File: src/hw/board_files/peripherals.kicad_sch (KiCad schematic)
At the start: 24 parts, among them J3 MSD-1-A, Q1 PMOS, U5 NEO-M9N, U6 BQ27427, U7 SHT30-DIS

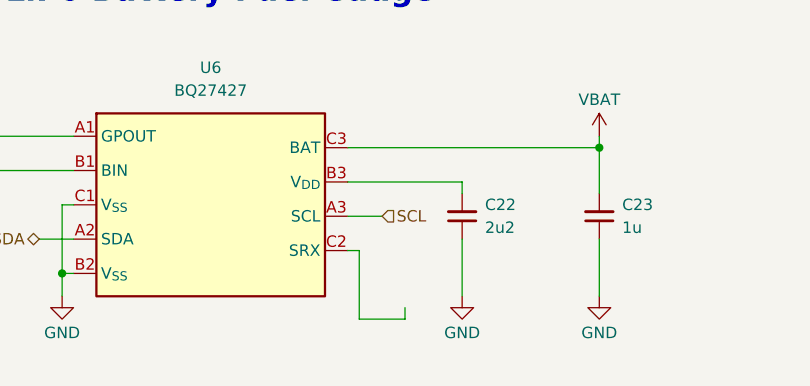
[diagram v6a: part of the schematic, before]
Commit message: Added more footprints and test points
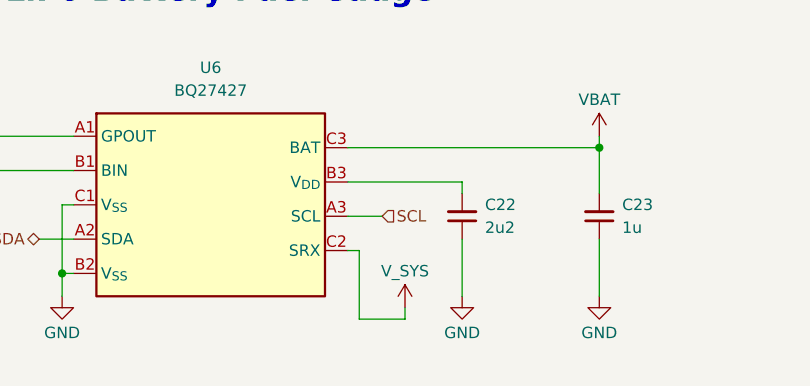
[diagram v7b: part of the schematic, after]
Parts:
- D7: footprint (none) -> LED_SMD:LED_0805_2012Metric_Pad1.15x1.40mm_HandSolder
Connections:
- net V_SYS: now reaches U6.C2 (SRX)
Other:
- title: Pocket Caddy -> Pocket Caddy - Golf GPS
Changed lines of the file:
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@@
 	(paper "A4")
 	(title_block
-		(title "Pocket Caddy")
-		(date "2025-09-25")
+		(title "Pocket Caddy - Golf GPS")
+		(date "2025-10-03")
 		(rev "0")
 		(company "EE 333 - Electronic Systems Design")
@@
 			)
 		)
-		(property "Footprint" ""
+		(property "Footprint" "LED_SMD:LED_0805_2012Metric_Pad1.15x1.40mm_HandSolder"
 			(at 52.07 69.85 0)
 			(effects
@@
 					(unit 1)
 				)
+			)
+		)
+	)
+	(symbol
+		(lib_id "power:+3V3")
+		(at 147.32 185.42 0)
+		(unit 1)
+		(exclude_from_sim no)
+		(in_bom yes)
+		(on_board yes)
+		(dnp no)
+		(property "Reference" "#PWR075"
+			(at 147.32 189.23 0)
+			(effects
+				(font
+					(size 1.27 1.27)
+				)
+				(hide yes)
+			)
+		)
+		(property "Value" "V_SYS"
+			(at 147.32 181.356 0)
+			(effects
+				(font
+					(size 1.27 1.27)
+				)
+			)
+		)
+		(property "Footprint" ""
+			(at 147.32 185.42 0)
+			(effects
+				(font
+					(size 1.27 1.27)
+				)
+				(hide yes)
+			)
+		)
+		(property "Datasheet" ""
+			(at 147.32 185.42 0)
+			(effects
+				(font
+					(size 1.27 1.27)
+				)
+				(hide yes)
+			)
+		)
+		(property "Description" "Power symbol creates a global label with name \"+3V3\""
+			(at 147.32 185.42 0)
+			(effects
+				(font
+					(size 1.27 1.27)
+				)
+				(hide yes)
+			)
+		)
+		(pin "1"
+		)
+		(instances
+			(project "pocket-caddy"
+				(path "/2c77a8ba-b277-4959-adec-d3fc778c7960/81382524-b053-4c3c-9e13-c8b314c52639"
+					(reference "#PWR075")
+					(unit 1)
+				)

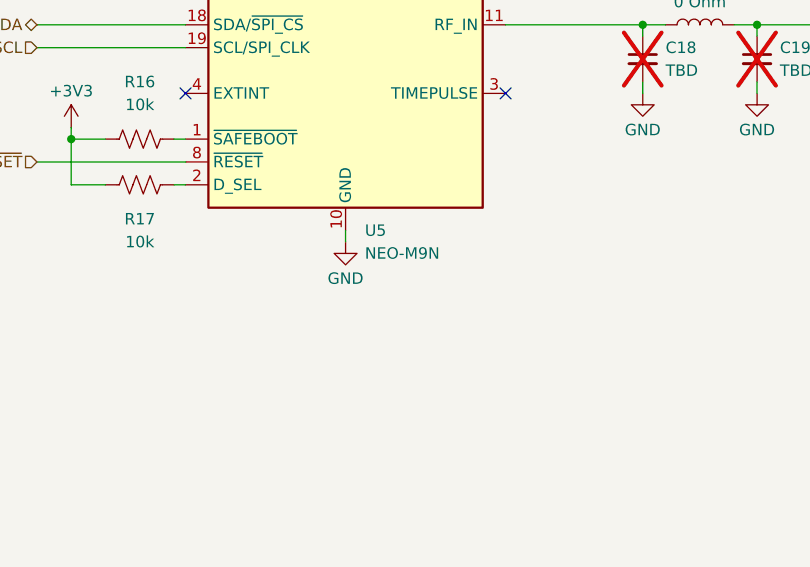
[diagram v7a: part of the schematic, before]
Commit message: Started Layout. Still Need Antenna & LCD Screen added
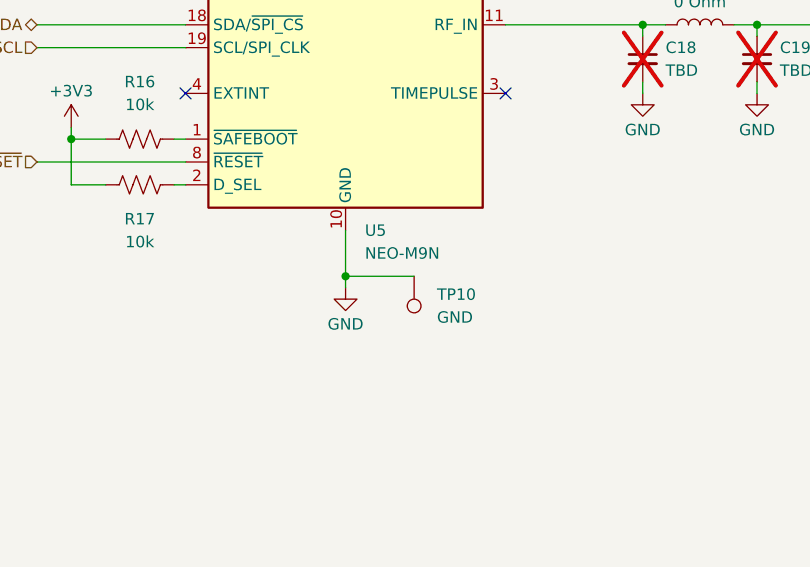
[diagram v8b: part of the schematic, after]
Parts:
- added TP10: GND, TestPoint:TestPoint_Loop_D2.54mm_Drill1.5mm_Beaded, symbol Connector:TestPoint
- J3: footprint (none) -> Library:CUI_MSD-1-A
- Q1: footprint (none) -> Library:SOT91P240X110-3N_DMG2305UX-7
- TP13: footprint (none) -> TestPoint:TestPoint_Loop_D2.54mm_Drill1.5mm_Beaded
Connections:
- net GND: now also TP10.1
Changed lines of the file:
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@@
 	)
 	(junction
+		(at 80.01 114.3)
+		(diameter 0)
+		(color 0 0 0 0)
+	)
+	(junction
 		(at 229.87 54.61)
 		(diameter 0)
@@
 	(wire
 		(pts
-			(xy 80.01 109.22) (xy 80.01 110.49)
+			(xy 80.01 109.22) (xy 80.01 114.3)
 		)
 		(stroke
@@
 	(wire
 		(pts
+			(xy 80.01 114.3) (xy 87.63 114.3)
+		)
+		(stroke
+			(width 0)
+			(type default)
+		)
+	)
+	(wire
+		(pts
 			(xy 50.8 168.91) (xy 50.8 165.1)
 		)
@@
 	(wire
 		(pts
+			(xy 80.01 114.3) (xy 80.01 115.57)
+		)
+		(stroke
+			(width 0)
+			(type default)
+		)
+	)
+	(wire
+		(pts
 			(xy 25.4 166.37) (xy 25.4 165.1)
 		)
@@
 			)
 		)
-		(property "Footprint" ""
+		(property "Footprint" "Library:CUI_MSD-1-A"
 			(at 289.56 111.76 0)
 			(effects
@@
 	)
 	(symbol
+		(lib_id "Connector:TestPoint")
+		(at 87.63 114.3 180)
+		(unit 1)
+		(exclude_from_sim no)
+		(in_bom yes)
+		(on_board yes)
+		(dnp no)
+		(fields_autoplaced yes)
+		(property "Reference" "TP10"
+			(at 90.17 116.3319 0)
+			(effects
+				(font
+					(size 1.27 1.27)
+				)
+				(justify right)
+			)
+		)
+		(property "Value" "GND"
+			(at 90.17 118.8719 0)
+			(effects
+				(font
+					(size 1.27 1.27)
+				)
+				(justify right)
+			)
+		)
+		(property "Footprint" "TestPoint:TestPoint_Loop_D2.54mm_Drill1.5mm_Beaded"
+			(at 82.55 114.3 0)
+			(effects
+				(font
+					(size 1.27 1.27)
+				)
+				(hide yes)
+			)
+		)
+		(property "Datasheet" "~"
+			(at 82.55 114.3 0)
+			(effects
+				(font
+					(size 1.27 1.27)
+				)
+				(hide yes)
+			)
+		)
+		(property "Description" "test point"
+			(at 87.63 114.3 0)
+			(effects
+				(font
+					(size 1.27 1.27)
+				)
+				(hide yes)
+			)
+		)
+		(pin "1"
+		)
+		(instances
+			(project "pocket-caddy"
+				(path "/2c77a8ba-b277-4959-adec-d3fc778c7960/81382524-b053-4c3c-9e13-c8b314c52639"
+					(reference "TP10")
+					(unit 1)
+				)
+			)
+		)
+	)
+	(symbol
 		(lib_id "power:GND")
 		(at 25.4 172.72 0)
@@
 	(symbol
 		(lib_id "power:GND")
-		(at 80.01 110.49 0)
+		(at 80.01 115.57 0)
 		(unit 1)
 		(exclude_from_sim no)
@@
 		(dnp no)
 		(property "Reference" "#PWR055"
-			(at 80.01 116.84 0)
+			(at 80.01 121.92 0)
 			(effects
 				(font
@@
 		)
 		(property "Value" "GND"
-			(at 80.01 114.554 0)
+			(at 80.01 119.634 0)
 			(effects
 				(font
@@
 		)
 		(property "Footprint" ""
-			(at 80.01 110.49 0)
+			(at 80.01 115.57 0)
 			(effects
 				(font
@@
 		)
 		(property "Datasheet" ""
-			(at 80.01 110.49 0)
+			(at 80.01 115.57 0)
 			(effects
 				(font
@@
 		)
 		(property "Description" "Power symbol creates a global label with name \"GND\" , ground"
-			(at 80.01 110.49 0)
+			(at 80.01 115.57 0)
 			(effects
 				(font
@@
 			)
 		)
-		(property "Footprint" ""
+		(property "Footprint" "TestPoint:TestPoint_Loop_D2.54mm_Drill1.5mm_Beaded"
 			(at 215.9 58.42 0)
 			(effects
@@
 			)
 		)
-		(property "Footprint" ""
+		(property "Footprint" "Library:SOT91P240X110-3N_DMG2305UX-7"
 			(at 38.1 53.34 0)
 			(effects
